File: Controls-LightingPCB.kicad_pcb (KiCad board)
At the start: 2 copper layers, 63.5 x 114.3 mm, 49 parts, among them J3 MinionConn, SW1 HAZARD, SW2 CRUISE_SET, SW3 CRUISE, SW4 F/R_SW, SW5 HEADLIGHT_SW, SW7 TURN_SIGNAL_SW, SW8 REGEN_SW, U3 MCP23S17_SS, U5 NCP1117-3.3_SOT223

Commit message: Adds gerbers and finalizes the new version
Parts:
- D1: moved to B.Cu
- moved D1 21.3 mm to (155.2, 149.3), turned to 0 degrees
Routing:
- net Net-(D1-Pad2): track 2.94 -> 17.6 mm, vias 0 -> 1
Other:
- board text added: "+"
- board text added: "-"
- board text added: "FOR"
- board text added: "Left"
- board text added: "Rev"
- board text added: "Right"
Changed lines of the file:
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@@
   (general
     (thickness 1.6)
-    (drawings 51)
-    (tracks 374)
+    (drawings 67)
+    (tracks 377)
     (zones 0)
     (modules 49)
@@
     (34 B.Paste user)
     (35 F.Paste user)
-    (36 B.SilkS user hide)
+    (36 B.SilkS user)
     (37 F.SilkS user)
     (38 B.Mask user)
@@
       (net 9 +3V3))
   )
-  (module LED_SMD:LED_0805_2012Metric (layer F.Cu)
-    (at 176.5 148.7 270)
+  (module LED_SMD:LED_0805_2012Metric (layer B.Cu)
+    (at 155.2 149.3)
     (descr "LED SMD 0805 (2012 Metric), square (rectangular) end terminal, IPC_7351 nominal, (Body size source: https://docs.google.com/spreadsheets/d/1BsfQQcO9C6DZCsRaXUlFlo91Tg2WpOkGARC1WS5S8t0/edit?usp=sharing), generated with kicad-footprint-generator")
     (tags diode)
     (attr smd)
-    (fp_text reference D1 (at 0 -1.65 90) (layer F.SilkS)
-      (effects (font (size 1 1) (thickness 0.15)))
+    (fp_text reference D1 (at 0 1.65) (layer B.SilkS)
+      (effects (font (size 1 1) (thickness 0.15)) (justify mirror))
     )
-    (fp_text value PowerOn (at 0 1.65 90) (layer F.Fab)
-      (effects (font (size 1 1) (thickness 0.15)))
+    (fp_text value PowerOn (at 0 -1.65) (layer B.Fab)
+      (effects (font (size 1 1) (thickness 0.15)) (justify mirror))
     )
-    (fp_text user %R (at 0 0 90) (layer F.Fab)
-      (effects (font (size 0.5 0.5) (thickness 0.08)))
+    (fp_text user %R (at 0 0) (layer B.Fab)
+      (effects (font (size 0.5 0.5) (thickness 0.08)) (justify mirror))
     )
-    (fp_line (start 1 -0.6) (end -0.7 -0.6) (layer F.Fab) (width 0.1))
-    (fp_line (start -0.7 -0.6) (end -1 -0.3) (layer F.Fab) (width 0.1))
-    (fp_line (start -1 -0.3) (end -1 0.6) (layer F.Fab) (width 0.1))
-    (fp_line (start -1 0.6) (end 1 0.6) (layer F.Fab) (width 0.1))
-    (fp_line (start 1 0.6) (end 1 -0.6) (layer F.Fab) (width 0.1))
-    (fp_line (start 1 -0.96) (end -1.685 -0.96) (layer F.SilkS) (width 0.12))
-    (fp_line (start -1.685 -0.96) (end -1.685 0.96) (layer F.SilkS) (width 0.12))
-    (fp_line (start -1.685 0.96) (end 1 0.96) (layer F.SilkS) (width 0.12))
-    (fp_line (start -1.68 0.95) (end -1.68 -0.95) (layer F.CrtYd) (width 0.05))
-    (fp_line (start -1.68 -0.95) (end 1.68 -0.95) (layer F.CrtYd) (width 0.05))
-    (fp_line (start 1.68 -0.95) (end 1.68 0.95) (layer F.CrtYd) (width 0.05))
-    (fp_line (start 1.68 0.95) (end -1.68 0.95) (layer F.CrtYd) (width 0.05))
-    (pad 2 smd roundrect (at 0.9375 0 270) (size 0.975 1.4) (layers F.Cu F.Paste F.Mask) (roundrect_rratio 0.25)
+    (fp_line (start 1 0.6) (end -0.7 0.6) (layer B.Fab) (width 0.1))
+    (fp_line (start -0.7 0.6) (end -1 0.3) (layer B.Fab) (width 0.1))
+    (fp_line (start -1 0.3) (end -1 -0.6) (layer B.Fab) (width 0.1))
+    (fp_line (start -1 -0.6) (end 1 -0.6) (layer B.Fab) (width 0.1))
+    (fp_line (start 1 -0.6) (end 1 0.6) (layer B.Fab) (width 0.1))
+    (fp_line (start 1 0.96) (end -1.685 0.96) (layer B.SilkS) (width 0.12))
+    (fp_line (start -1.685 0.96) (end -1.685 -0.96) (layer B.SilkS) (width 0.12))
+    (fp_line (start -1.685 -0.96) (end 1 -0.96) (layer B.SilkS) (width 0.12))
+    (fp_line (start -1.68 -0.95) (end -1.68 0.95) (layer B.CrtYd) (width 0.05))
+    (fp_line (start -1.68 0.95) (end 1.68 0.95) (layer B.CrtYd) (width 0.05))
+    (fp_line (start 1.68 0.95) (end 1.68 -0.95) (layer B.CrtYd) (width 0.05))
+    (fp_line (start 1.68 -0.95) (end -1.68 -0.95) (layer B.CrtYd) (width 0.05))
+    (pad 2 smd roundrect (at 0.9375 0) (size 0.975 1.4) (layers B.Cu B.Paste B.Mask) (roundrect_rratio 0.25)
       (net 14 "Net-(D1-Pad2)"))
-    (pad 1 smd roundrect (at -0.9375 0 270) (size 0.975 1.4) (layers F.Cu F.Paste F.Mask) (roundrect_rratio 0.25)
+    (pad 1 smd roundrect (at -0.9375 0) (size 0.975 1.4) (layers B.Cu B.Paste B.Mask) (roundrect_rratio 0.25)
       (net 10 GND))
     (model ${KISYS3DMOD}/LED_SMD.3dshapes/LED_0805_2012Metric.wrl
@@
     )
   )
+  (gr_text Right (at 171.9 72.4) (layer F.SilkS)
+    (effects (font (size 1 1) (thickness 0.15)))
+  )
+  (gr_text GND (at 171.9 75.4) (layer F.SilkS)
+    (effects (font (size 1 1) (thickness 0.15)))
+  )
+  (gr_text Left (at 172 78.3) (layer F.SilkS)
+    (effects (font (size 1 1) (thickness 0.15)))
+  )
+  (gr_text - (at 175.2 86.5) (layer F.SilkS)
+    (effects (font (size 1 1) (thickness 0.15)))
+  )
+  (gr_text + (at 175.2 94.8) (layer F.SilkS)
+    (effects (font (size 1 1) (thickness 0.15)))
+  )
+  (gr_text - (at 173.8 102.9) (layer F.SilkS)
+    (effects (font (size 1 1) (thickness 0.15)))
+  )
+  (gr_text + (at 173.8 105.9) (layer F.SilkS)
+    (effects (font (size 1 1) (thickness 0.15)))
+  )
+  (gr_text - (at 175.5 113.4) (layer F.SilkS)
+    (effects (font (size 1 1) (thickness 0.15)))
+  )
+  (gr_text + (at 175.5 122.7) (layer F.SilkS)
+    (effects (font (size 1 1) (thickness 0.15)))
+  )
+  (gr_text - (at 175.5 129.1) (layer F.SilkS)
+    (effects (font (size 1 1) (thickness 0.15)))
+  )
+  (gr_text + (at 175.5 134.4) (layer F.SilkS)
+    (effects (font (size 1 1) (thickness 0.15)))
+  )
+  (gr_text - (at 138.4 125.8) (layer F.SilkS)
+    (effects (font (size 1 1) (thickness 0.15)))
+  )
+  (gr_text + (at 138.4 122.8) (layer F.SilkS)
+    (effects (font (size 1 1) (thickness 0.15)))
+  )
+  (gr_text FOR (at 139.8 113.7) (layer F.SilkS)
+    (effects (font (size 1 1) (thickness 0.15)))
+  )
+  (gr_text GND (at 139.8 110.7) (layer F.SilkS)
+    (effects (font (size 1 1) (thickness 0.15)))
+  )
+  (gr_text Rev (at 139.7 107.6) (layer F.SilkS)
+    (effects (font (size 1 1) (thickness 0.15)))
+  )
   (gr_text "Aaron\nwas\nhere" (at 183.5 79.3 270) (layer F.SilkS)
     (effects (font (size 1 1) (thickness 0.15)))
@@
   (segment (start 176.4185 145.5575) (end 176.497 145.636) (width 0.25) (layer F.Cu) (net 13))
   (segment (start 173.703 145.5575) (end 176.4185 145.5575) (width 0.25) (layer F.Cu) (net 13))
-  (segment (start 176.5755 149.7485) (end 176.624 149.797) (width 0.25) (layer F.Cu) (net 14))
-  (segment (start 173.703 149.7485) (end 176.5755 149.7485) (width 0.25) (layer F.Cu) (net 14))
+  (segment (start 173.576 149.6215) (end 171.7215 149.6215) (width 0.25) (layer F.Cu) (net 14))
+  (via (at 171.7 149.6) (size 0.8) (drill 0.4) (layers F.Cu B.Cu) (net 14))
+  (segment (start 171.7215 149.6215) (end 171.7 149.6) (width 0.25) (layer F.Cu) (net 14))
+  (segment (start 156.4375 149.6) (end 156.1375 149.3) (width 0.25) (layer B.Cu) (net 14))
+  (segment (start 171.7 149.6) (end 156.4375 149.6) (width 0.25) (layer B.Cu) (net 14))
   (segment (start 166.538973 68.053527) (end 167.0245 67.568) (width 0.25) (layer B.Cu) (net 15))
   (segment (start 156 69) (end 165.5925 69) (width 0.25) (layer B.Cu) (net 15))

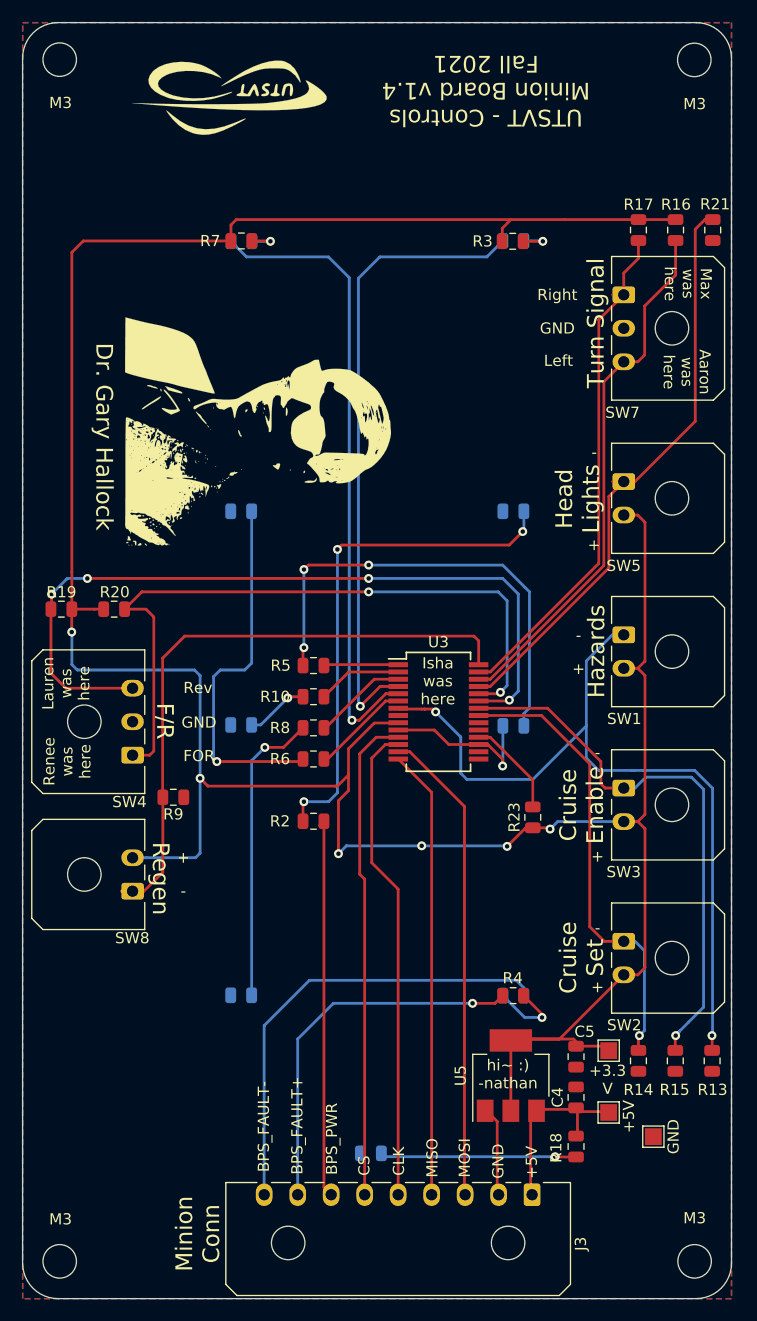
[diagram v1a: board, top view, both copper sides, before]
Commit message: Fix issue with LED
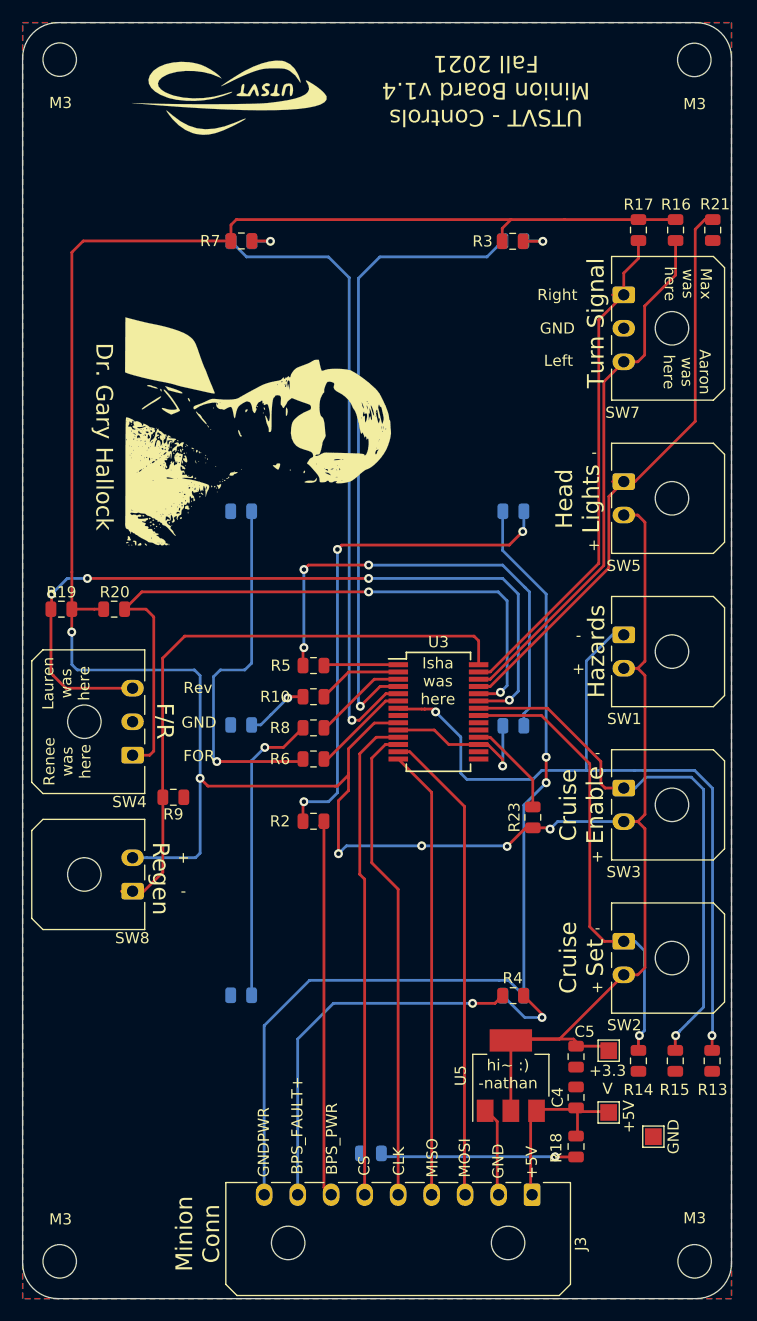
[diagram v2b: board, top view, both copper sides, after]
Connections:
- D2 pad 1: GND -> GNDPWR
- D4 pad 1: /BPS_FAULT- -> GNDPWR
- J3 pad 9: /BPS_FAULT- -> GNDPWR
- U3 pad 19: Net-(U3-Pad19) -> unconnected-(U3-Pad19)
- U3 pad 20: Net-(U3-Pad20) -> unconnected-(U3-Pad20)
- U3 pad 8: Net-(U3-Pad8) -> unconnected-(U3-Pad8)
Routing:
- net GNDPWR: track 0.00 -> 86.5 mm, vias 0 -> 2
- net /BPS_FAULT-: track 41.1 -> 0.00 mm
- net /HZD_SW: track 73.0 -> 71.7 mm
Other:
- net class Default removed
- board text added: "GNDPWR"
- board text added: "hi~ :) -nathan"
- board text removed: "BPS_FAULT-"
- board text removed: "hi~~ :) -nathan"

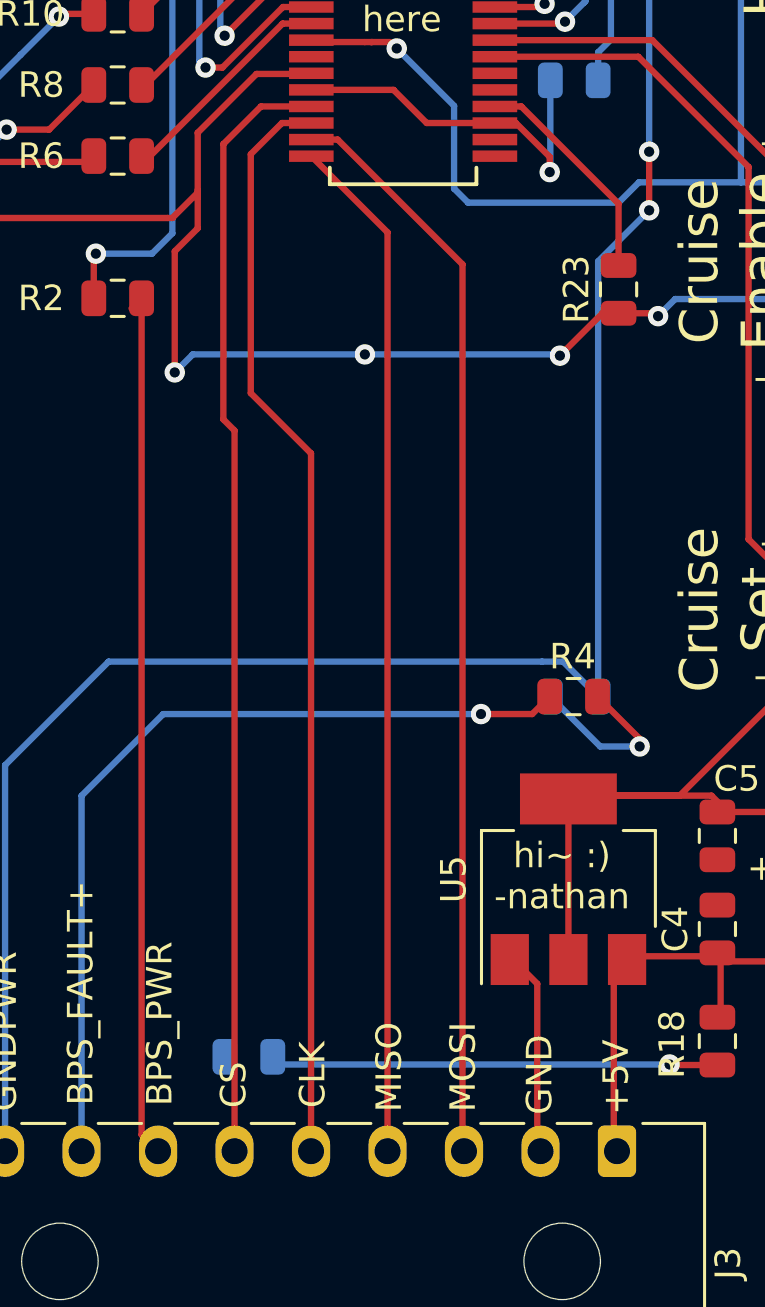
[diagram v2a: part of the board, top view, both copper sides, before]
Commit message: Adds 60ohm resistor to MISO line
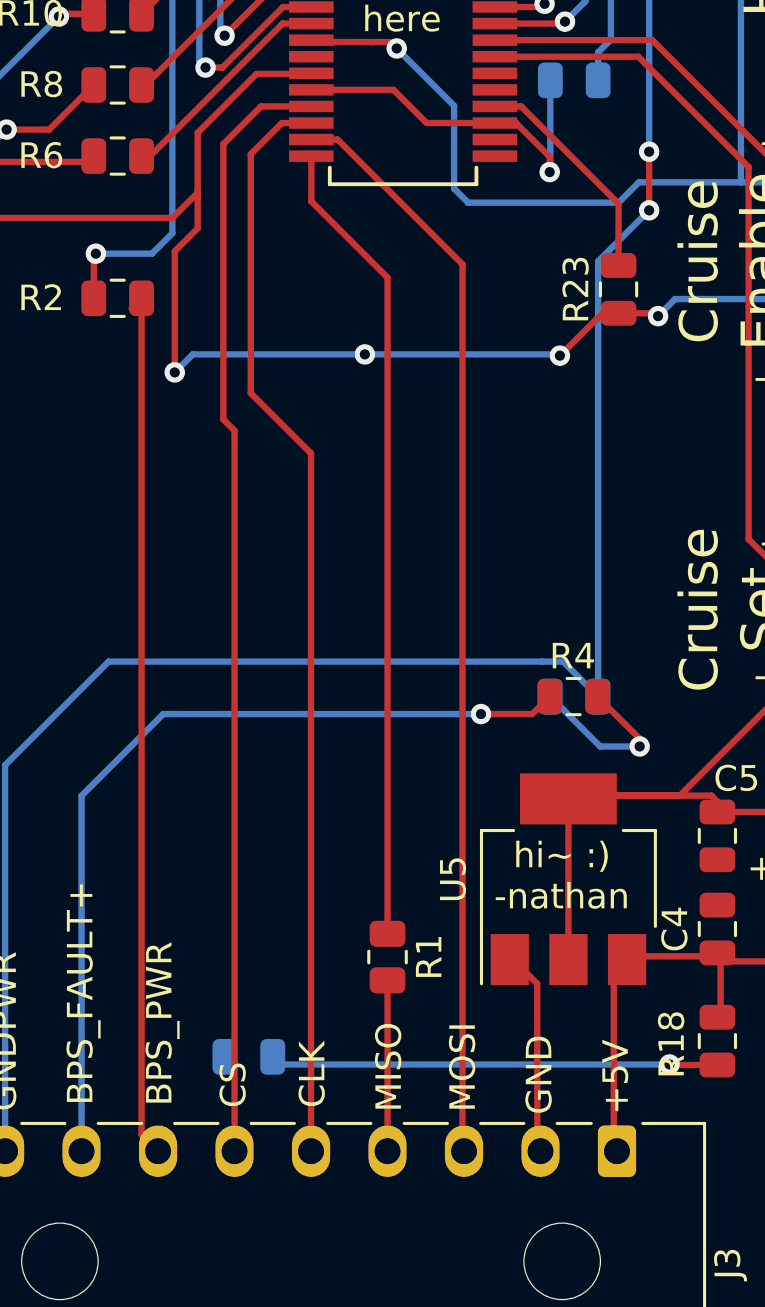
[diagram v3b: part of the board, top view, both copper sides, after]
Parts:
- added R1: 60, Resistor_SMD:R_0805_2012Metric, F.Cu at (160.6, 145.4)
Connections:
- J3 pad 4: /MISO -> Net-(J3-Pad4)
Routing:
- net /MISO: track 40.7 -> 32.2 mm
- net Net-(J3-Pad4): track 0.00 -> 6.70 mm
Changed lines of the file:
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@@
   (net 37 "unconnected-(U3-Pad8)")
   (net 38 "Net-(R23-Pad2)")
+  (net 39 "Net-(J3-Pad4)")
   (footprint "Resistor_SMD:R_0805_2012Metric" (layer "F.Cu")
     (at 150.0556 108.39364 180)
@@
       (net 31 "/MOSI") (pinfunction "Pin_3") (pintype "passive"))
     (pad "4" thru_hole oval locked (at 9 0 180) (size 1.5 2.02) (drill 1.02) (layers *.Cu *.Mask)
-      (net 32 "/MISO") (pinfunction "Pin_4") (pintype "passive"))
+      (net 39 "Net-(J3-Pad4)") (pinfunction "Pin_4") (pintype "passive"))
     (pad "5" thru_hole oval locked (at 12 0 180) (size 1.5 2.02) (drill 1.02) (layers *.Cu *.Mask)
       (net 33 "/SCK") (pinfunction "Pin_5") (pintype "passive"))
@@
     )
   )
+  (footprint "Resistor_SMD:R_0805_2012Metric" (layer "F.Cu")
+    (at 160.639 145.3875 -90)
+    (descr "Resistor SMD 0805 (2012 Metric), square (rectangular) end terminal, IPC_7351 nominal, (Body size source: IPC-SM-782 page 72, https://www.pcb-3d.com/wordpress/wp-content/uploads/ipc-sm-782a_amendment_1_and_2.pdf), generated with kicad-footprint-generator")
+    (tags "resistor")
+    (property "Sheetfile" "Controls-LightingPCB.kicad_sch")
+    (property "Sheetname" "")
+    (attr smd)
+    (fp_text reference "R1" (at 0 -1.65 90) (layer "F.SilkS")
+      (effects (font (size 1 1) (thickness 0.15)))
+    )
+    (fp_text value "60" (at 0 1.65 90) (layer "F.Fab")
+      (effects (font (size 1 1) (thickness 0.15)))
+    )
+    (fp_text user "${REFERENCE}" (at 0 0 90) (layer "F.Fab")
+      (effects (font (size 0.5 0.5) (thickness 0.08)))
+    )
+    (fp_line (start -0.227064 -0.735) (end 0.227064 -0.735) (layer "F.SilkS") (width 0.12))
+    (fp_line (start -0.227064 0.735) (end 0.227064 0.735) (layer "F.SilkS") (width 0.12))
+    (fp_line (start 1.68 0.95) (end -1.68 0.95) (layer "F.CrtYd") (width 0.05))
+    (fp_line (start 1.68 -0.95) (end 1.68 0.95) (layer "F.CrtYd") (width 0.05))
+    (fp_line (start -1.68 0.95) (end -1.68 -0.95) (layer "F.CrtYd") (width 0.05))
+    (fp_line (start -1.68 -0.95) (end 1.68 -0.95) (layer "F.CrtYd") (width 0.05))
+    (fp_line (start -1 -0.625) (end 1 -0.625) (layer "F.Fab") (width 0.1))
+    (fp_line (start 1 0.625) (end -1 0.625) (layer "F.Fab") (width 0.1))
+    (fp_line (start -1 0.625) (end -1 -0.625) (layer "F.Fab") (width 0.1))
+    (fp_line (start 1 -0.625) (end 1 0.625) (layer "F.Fab") (width 0.1))
+    (pad "1" smd roundrect (at -0.9125 0 270) (size 1.025 1.4) (layers "F.Cu" "F.Paste" "F.Mask") (roundrect_rratio 0.243902)
+      (net 32 "/MISO") (pintype "passive"))
+    (pad "2" smd roundrect (at 0.9125 0 270) (size 1.025 1.4) (layers "F.Cu" "F.Paste" "F.Mask") (roundrect_rratio 0.243902)
+      (net 39 "Net-(J3-Pad4)") (pintype "passive"))
+    (model "${KICAD6_3DMODEL_DIR}/Resistor_SMD.3dshapes/R_0805_2012Metric.wrl"
+      (offset (xyz 0 0 0))
+      (scale (xyz 1 1 1))
+      (rotate (xyz 0 0 0))
+    )
+  )
   (footprint "Diode_SMD:D_0805_2012Metric" (layer "B.Cu")
     (at 143.578 135.1377)
@@
   (segment (start 158.685002 113.325) (end 157.65 113.325) (width 0.25) (layer "F.Cu") (net 31))
   (segment (start 163.579999 118.219997) (end 158.685002 113.325) (width 0.25) (layer "F.Cu") (net 31))
-  (segment (start 160.639 116.964) (end 157.65 113.975) (width 0.25) (layer "F.Cu") (net 32))
-  (segment (start 160.639 153.002) (end 160.639 116.964) (width 0.25) (layer "F.Cu") (net 32))
+  (segment (start 160.639 144.475) (end 160.639 118.739) (width 0.25) (layer "F.Cu") (net 32))
+  (segment (start 157.65 115.75) (end 157.65 113.975) (width 0.25) (layer "F.Cu") (net 32))
   (segment (start 157.65 113.975) (end 157.193609 113.975) (width 0.25) (layer "F.Cu") (net 32))
+  (segment (start 160.639 118.739) (end 157.65 115.75) (width 0.25) (layer "F.Cu") (net 32))
   (segment (start 157.639 125.63359) (end 155.27499 123.26958) (width 0.25) (layer "F.Cu") (net 33))
   (segment (start 155.27499 113.89901) (end 156.499 112.675) (width 0.25) (layer "F.Cu") (net 33))
@@
   (segment (start 164.85 112.025) (end 165.885002 112.025) (width 0.25) (layer "F.Cu") (net 38))
   (segment (start 169.7 115.839998) (end 169.7 118.2625) (width 0.25) (layer "F.Cu") (net 38))
+  (segment (start 160.639 153.002) (end 160.639 146.3) (width 0.25) (layer "F.Cu") (net 39))
   (zone (net 10) (net_name "GND") (layer "F.Cu") (hatch edge 0.508)
     (connect_pads yes (clearance 0.508))
